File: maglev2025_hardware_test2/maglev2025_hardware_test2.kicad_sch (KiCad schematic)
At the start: 186 parts, among them J1 SWD, J2 PWRIn, J3 Conn_01x04, J4 Conn_01x04_MountingPin, J5 USB_C_Receptacle_USB2.0, J6 Conn_01x04, Q1 AO3400A, SW4 RotaryEncoder_Switch_MP, U1 RY8411, U10 INA240A1PW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

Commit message: finish layout, checking in progress
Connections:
- net +5V is gone; now on net +5V_BLINK: C55.1, J4.3 (Pin_3)
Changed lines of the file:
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@@
 	)
 	(junction
+		(at 78.486 -118.9658)
+		(diameter 0)
+		(color 0 0 0 0)
+	)
+	(junction
 		(at 48.26 43.18)
 		(diameter 0)
@@
 	(wire
 		(pts
+			(xy 78.486 -118.9658) (xy 78.486 -117.856)
+		)
+		(stroke
+			(width 0)
+			(type default)
+		)
+	)
+	(wire
+		(pts
 			(xy 93.98 196.85) (xy 93.98 195.58)
 		)
@@
 	(wire
 		(pts
-			(xy 78.486 -119.126) (xy 78.486 -117.856)
+			(xy 78.486 -119.126) (xy 78.486 -118.9658)
 		)
 		(stroke
@@
 	)
 	(symbol
+		(lib_id "power:+5V")
+		(at 98.806 -114.046 0)
+		(unit 1)
+		(exclude_from_sim no)
+		(in_bom yes)
+		(on_board yes)
+		(dnp no)
+		(fields_autoplaced yes)
+		(property "Reference" "#PWR085"
+			(at 98.806 -110.236 0)
+			(effects
+				(font
+					(size 1.27 1.27)
+				)
+				(hide yes)
+			)
+		)
+		(property "Value" "+5V_BLINK"
+			(at 98.806 -119.126 0)
+			(effects
+				(font
+					(size 1.27 1.27)
+				)
+			)
+		)
+		(property "Footprint" ""
+			(at 98.806 -114.046 0)
+			(effects
+				(font
+					(size 1.27 1.27)
+				)
+				(hide yes)
+			)
+		)
+		(property "Datasheet" ""
+			(at 98.806 -114.046 0)
+			(effects
+				(font
+					(size 1.27 1.27)
+				)
+				(hide yes)
+			)
+		)
+		(property "Description" "Power symbol creates a global label with name \"+5V\""
+			(at 98.806 -114.046 0)
+			(effects
+				(font
+					(size 1.27 1.27)
+				)
+				(hide yes)
+			)
+		)
+		(pin "1"
+		)
+		(instances
+			(project "maglev2025_hardware_test2"
+				(path "/0d07820d-bdd1-4a97-9f99-c901fa8e1338"
+					(reference "#PWR085")
+					(unit 1)
+				)
+			)
+		)
+	)
+	(symbol
 		(lib_id "Device:C")
 		(at 41.91 46.99 90)
@@
 	)
 	(symbol
-		(lib_id "power:+5V")
-		(at 98.806 -114.046 90)
-		(unit 1)
-		(exclude_from_sim no)
-		(in_bom yes)
-		(on_board yes)
-		(dnp no)
-		(fields_autoplaced yes)
-		(property "Reference" "#PWR088"
-			(at 102.616 -114.046 0)
-			(effects
-				(font
-					(size 1.27 1.27)
-				)
-				(hide yes)
-			)
-		)
-		(property "Value" "+5V"
-			(at 94.996 -114.0461 90)
-			(effects
-				(font
-					(size 1.27 1.27)
-				)
-				(justify left)
-			)
-		)
-		(property "Footprint" ""
-			(at 98.806 -114.046 0)
-			(effects
-				(font
-					(size 1.27 1.27)
-				)
-				(hide yes)
-			)
-		)
-		(property "Datasheet" ""
-			(at 98.806 -114.046 0)
-			(effects
-				(font
-					(size 1.27 1.27)
-				)
-				(hide yes)
-			)
-		)
-		(property "Description" "Power symbol creates a global label with name \"+5V\""
-			(at 98.806 -114.046 0)
-			(effects
-				(font
-					(size 1.27 1.27)
-				)
-				(hide yes)
-			)
-		)
-		(pin "1"
-		)
-		(instances
-			(project "maglev2025_hardware_test2"
-				(path "/0d07820d-bdd1-4a97-9f99-c901fa8e1338"
-					(reference "#PWR088")
-					(unit 1)
-				)
-			)
-		)
-	)
-	(symbol
 		(lib_id "power:+3.3V")
 		(at 377.19 125.73 0)
@@
 	(symbol
 		(lib_id "power:+5V")
+		(at 78.486 -118.9658 0)
+		(unit 1)
+		(exclude_from_sim no)
+		(in_bom yes)
+		(on_board yes)
+		(dnp no)
+		(fields_autoplaced yes)
+		(property "Reference" "#PWR084"
+			(at 78.486 -115.1558 0)
+			(effects
+				(font
+					(size 1.27 1.27)
+				)
+				(hide yes)
+			)
+		)
+		(property "Value" "+5V_BLINK"
+			(at 78.486 -124.0458 0)
+			(effects
+				(font
+					(size 1.27 1.27)
+				)
+			)
+		)
+		(property "Footprint" ""
+			(at 78.486 -118.9658 0)
+			(effects
+				(font
+					(size 1.27 1.27)
+				)
+				(hide yes)
+			)
+		)
+		(property "Datasheet" ""
+			(at 78.486 -118.9658 0)
+			(effects
+				(font
+					(size 1.27 1.27)
+				)
+				(hide yes)
+			)
+		)
+		(property "Description" "Power symbol creates a global label with name \"+5V\""
+			(at 78.486 -118.9658 0)
+			(effects
+				(font
+					(size 1.27 1.27)
+				)
+				(hide yes)
+			)
+		)
+		(pin "1"
+		)
+		(instances
+			(project "maglev2025_hardware_test2"
+				(path "/0d07820d-bdd1-4a97-9f99-c901fa8e1338"
+					(reference "#PWR084")
+					(unit 1)
+				)
+			)
+		)
+	)
+	(symbol
+		(lib_id "power:+5V")
 		(at 251.46 267.97 0)
 		(unit 1)
@@
 					(unit 1)
 				)
-			)
-		)
-	)
-	(symbol
-		(lib_id "power:+5V")
-		(at 78.486 -119.126 90)
-		(unit 1)
-		(exclude_from_sim no)
-		(in_bom yes)
-		(on_board yes)
-		(dnp no)
-		(fields_autoplaced yes)
-		(property "Reference" "#PWR090"
-			(at 82.296 -119.126 0)
-			(effects
-				(font
-					(size 1.27 1.27)
-				)
-				(hide yes)
-			)
-		)
-		(property "Value" "+5V"
-			(at 74.676 -119.1261 90)
-			(effects
-				(font
-					(size 1.27 1.27)
-				)
-				(justify left)
-			)
-		)
-		(property "Footprint" ""
-			(at 78.486 -119.126 0)
-			(effects
-				(font
-					(size 1.27 1.27)
-				)
-				(hide yes)
-			)
-		)
-		(property "Datasheet" ""
-			(at 78.486 -119.126 0)
-			(effects
-				(font
-					(size 1.27 1.27)
-				)
-				(hide yes)
-			)
-		)
-		(property "Description" "Power symbol creates a global label with name \"+5V\""
-			(at 78.486 -119.126 0)
-			(effects
-				(font
-					(size 1.27 1.27)
-				)
-				(hide yes)
-			)
-		)
-		(pin "1"
-		)
-		(instances
-			(project "maglev2025_hardware_test2"
-				(path "/0d07820d-bdd1-4a97-9f99-c901fa8e1338"
-					(reference "#PWR090")
-					(unit 1)
-				)

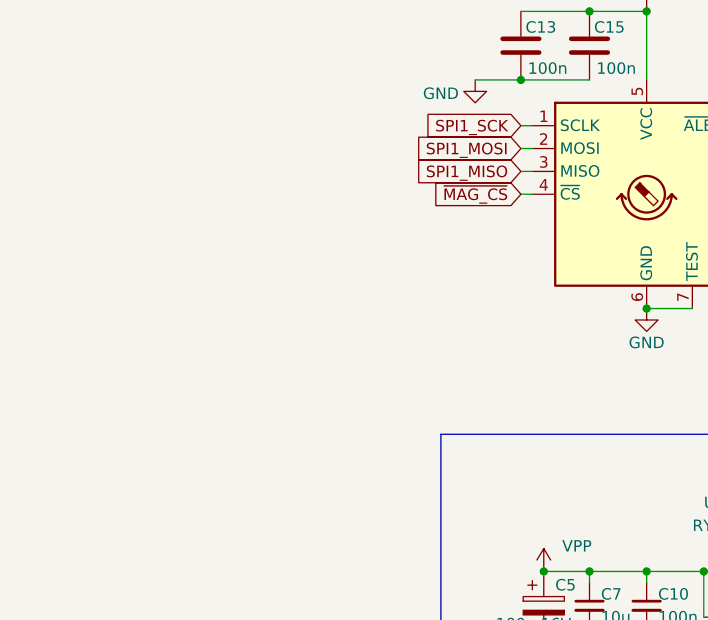
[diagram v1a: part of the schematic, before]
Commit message: adding external hal connector
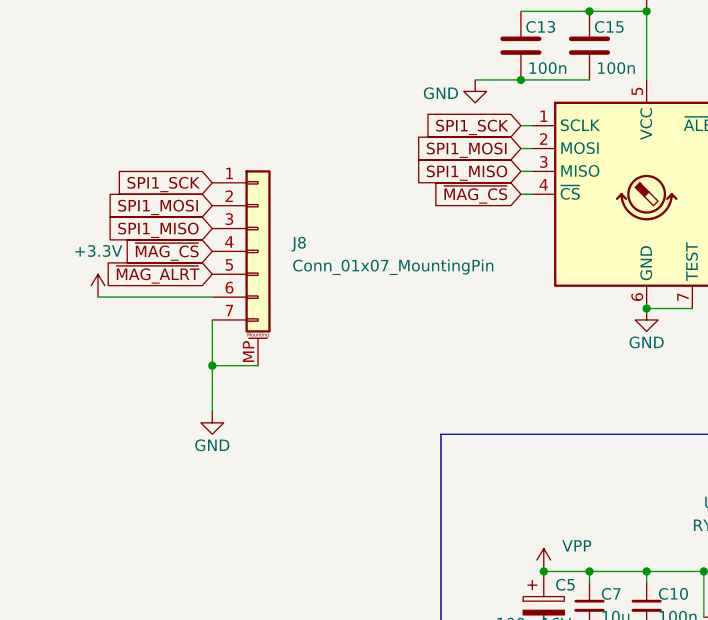
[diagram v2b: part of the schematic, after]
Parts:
- added J8: Conn_01x07_MountingPin, Connector_JST:JST_GH_SM07B-GHS-TB_1x07-1MP_P1.25mm_Horizontal, symbol Connector_Generic_MountingPin:Conn_01x07_MountingPin
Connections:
- net +3.3V: now also J8.6 (Pin_6)
- net GND: now also J8.7 (Pin_7), J8.MP (MountPin)
- net SPI1_MISO: now also J8.3 (Pin_3)
- net SPI1_MOSI: now also J8.2 (Pin_2)
- net SPI1_SCK: now also J8.1 (Pin_1)
- net ~{MAG_ALRT}: now also J8.5 (Pin_5)
- net ~{MAG_CS}: now also J8.4 (Pin_4)

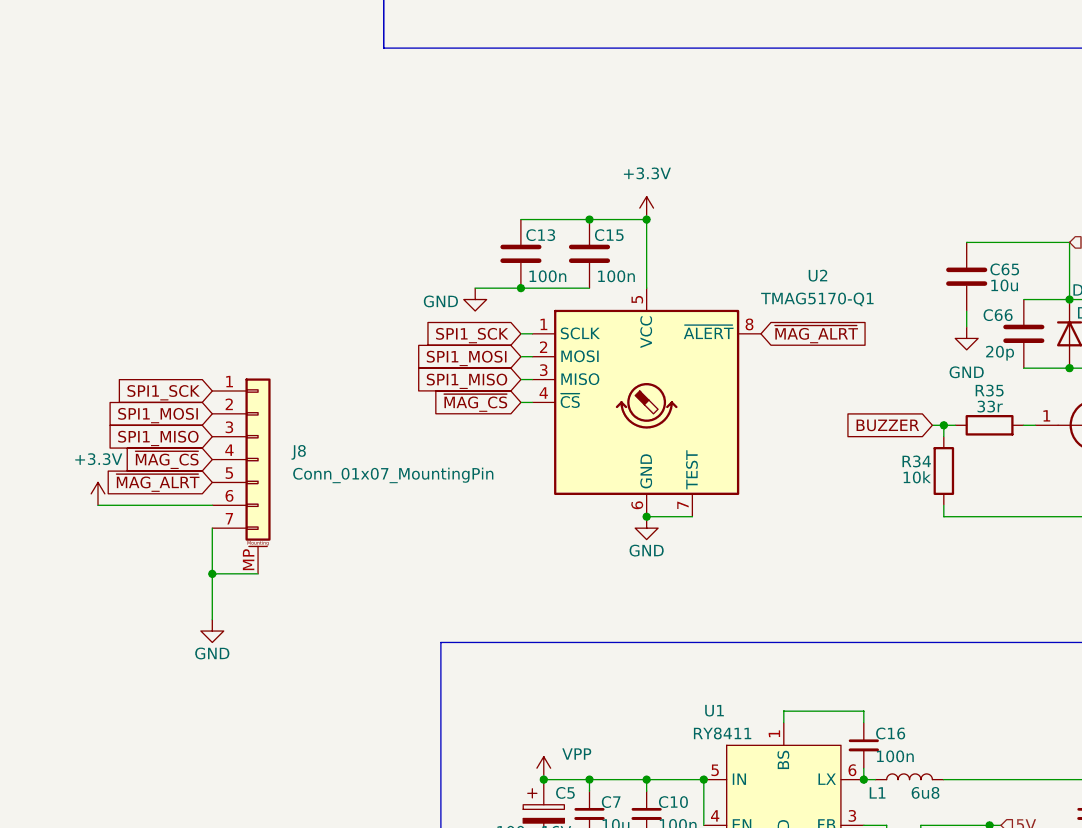
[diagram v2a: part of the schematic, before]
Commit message: modify layout
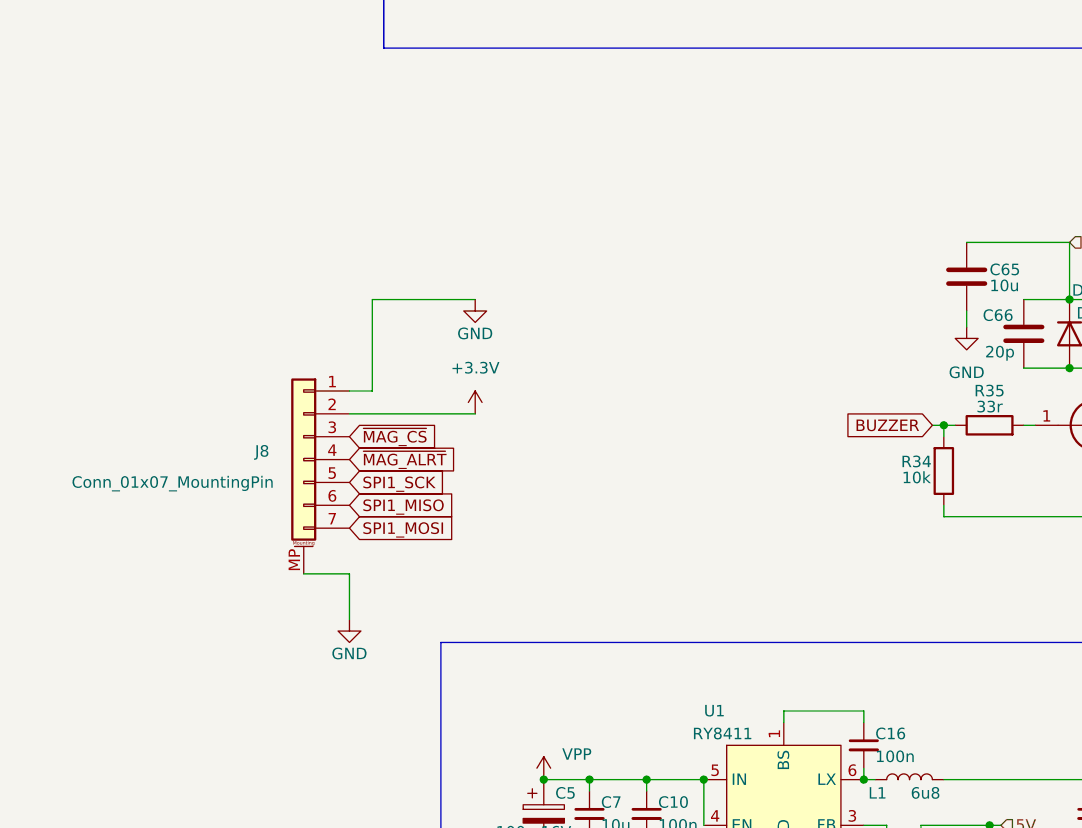
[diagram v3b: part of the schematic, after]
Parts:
- removed C13, C15: 100n, Capacitor_SMD:C_0603_1608Metric, symbol Device:C
- removed U2: TMAG5170-Q1, Package_SO:VSSOP-8_3x3mm_P0.65mm, symbol Sensor_Magnetic:TMAG5170-Q1
- L6: footprint Inductor_SMD:L_Sunlord_MWSA0402S -> Inductor_SMD:L_Chilisin_BMRx00060630
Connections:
- net +3.3V: now also J8.2 (Pin_2); no longer J8.6 (Pin_6)
- net GND: now also J8.1 (Pin_1); no longer J8.7 (Pin_7)
- net SPI1_MISO: now also J8.6 (Pin_6); no longer J8.3 (Pin_3)
- net SPI1_MOSI: now also J8.7 (Pin_7); no longer J8.2 (Pin_2)
- net SPI1_SCK: now also J8.5 (Pin_5); no longer J8.1 (Pin_1)
- net ~{MAG_ALRT}: now also J8.4 (Pin_4); no longer J8.5 (Pin_5)
- net ~{MAG_CS}: now also J8.3 (Pin_3); no longer J8.4 (Pin_4)
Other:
- moved on the sheet: J8

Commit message: modify layout
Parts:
- removed H1, H4: MountingHole_Pad, MountingHole:MountingHole_3.2mm_M3_DIN965_Pad_TopBottom, symbol Mechanical:MountingHole_Pad
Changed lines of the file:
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@@
-	)
-	(symbol
-		(lib_id "Mechanical:MountingHole_Pad")
-		(at 375.92 162.56 0)
-		(unit 1)
-		(exclude_from_sim yes)
-		(in_bom no)
-		(on_board yes)
-		(dnp no)
-		(fields_autoplaced yes)
-		(property "Reference" "H1"
-			(at 378.46 160.0199 0)
-			(effects
-				(font
-					(size 1.27 1.27)
-				)
-				(justify left)
-			)
-		)
-		(property "Value" "MountingHole_Pad"
-			(at 378.46 162.5599 0)
-			(effects
-				(font
-					(size 1.27 1.27)
-				)
-				(justify left)
-			)
-		)
-		(property "Footprint" "MountingHole:MountingHole_3.2mm_M3_DIN965_Pad_TopBottom"
-			(at 375.92 162.56 0)
-			(effects
-				(font
-					(size 1.27 1.27)
-				)
-				(hide yes)
-			)
-		)
-		(property "Datasheet" "~"
-			(at 375.92 162.56 0)
-			(effects
-				(font
-					(size 1.27 1.27)
-				)
-				(hide yes)
-			)
-		)
-		(property "Description" "Mounting Hole with connection"
-			(at 375.92 162.56 0)
-			(effects
-				(font
-					(size 1.27 1.27)
-				)
-				(hide yes)
-			)
-		)
-		(pin "1"
-		)
-		(instances
-			(project ""
-				(path "/0d07820d-bdd1-4a97-9f99-c901fa8e1338"
-					(reference "H1")
-					(unit 1)
-				)
-			)
-		)
 	)
 	(symbol
@@
 					(unit 1)
 				)
-			)
-		)
-	)
-	(symbol
-		(lib_id "Mechanical:MountingHole_Pad")
-		(at 375.92 185.42 0)
-		(unit 1)
-		(exclude_from_sim yes)
-		(in_bom no)
-		(on_board yes)
-		(dnp no)
-		(fields_autoplaced yes)
-		(property "Reference" "H4"
-			(at 378.46 182.8799 0)
-			(effects
-				(font
-					(size 1.27 1.27)
-				)
-				(justify left)
-			)
-		)
-		(property "Value" "MountingHole_Pad"
-			(at 378.46 185.4199 0)
-			(effects
-				(font
-					(size 1.27 1.27)
-				)
-				(justify left)
-			)
-		)
-		(property "Footprint" "MountingHole:MountingHole_3.2mm_M3_DIN965_Pad_TopBottom"
-			(at 375.92 185.42 0)
-			(effects
-				(font
-					(size 1.27 1.27)
-				)
-				(hide yes)
-			)
-		)
-		(property "Datasheet" "~"
-			(at 375.92 185.42 0)
-			(effects
-				(font
-					(size 1.27 1.27)
-				)
-				(hide yes)
-			)
-		)
-		(property "Description" "Mounting Hole with connection"
-			(at 375.92 185.42 0)
-			(effects
-				(font
-					(size 1.27 1.27)
-				)
-				(hide yes)
-			)
-		)
-		(pin "1"
-		)
-		(instances
-			(project "maglev2025_hardware_test1"
-				(path "/0d07820d-bdd1-4a97-9f99-c901fa8e1338"
-					(reference "H4")
-					(unit 1)
-				)
